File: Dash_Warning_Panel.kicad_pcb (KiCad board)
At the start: 2 copper layers, 57 x 40 mm, 30 parts, among them J1 Conn_01x06_Male, SW1 SW_DIP_x02, U1 BD2808MUV, U3 TPS22810-Q1

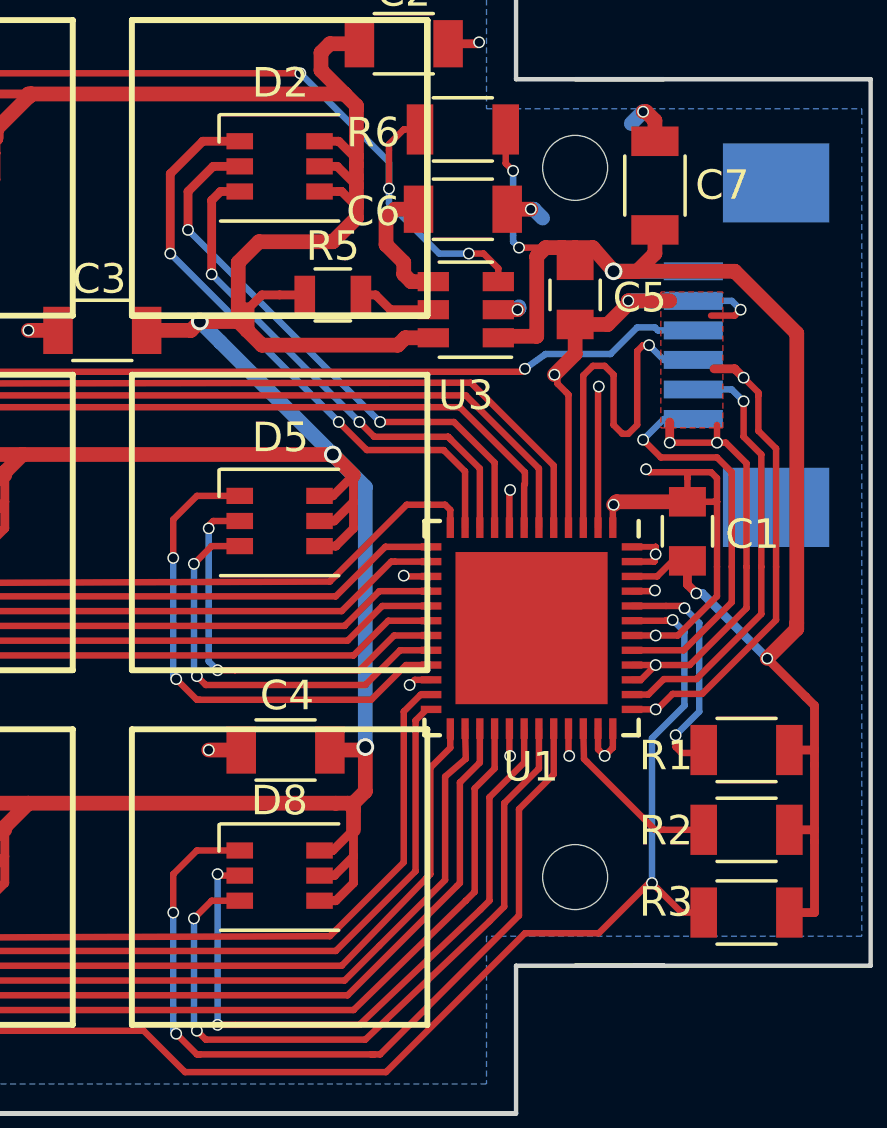
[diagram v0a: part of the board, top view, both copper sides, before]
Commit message: Fixed C6 footprint
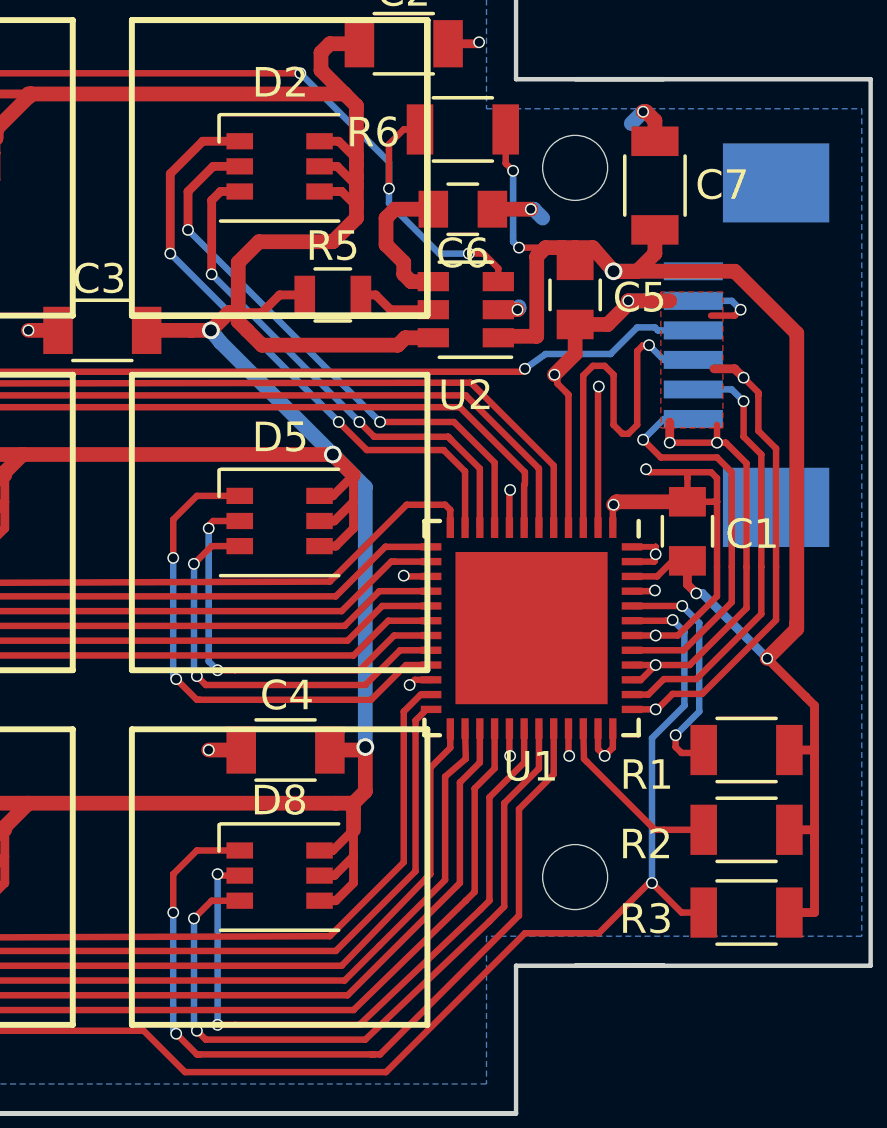
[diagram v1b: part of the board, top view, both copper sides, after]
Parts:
- C6: footprint Capacitors_SMD:C_1206 -> Capacitors_SMD:C_0805
- R2: value 10k -> 68k
- renumbered U3 to U2
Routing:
- net /LED_Power: track 174.0 -> 173.5 mm

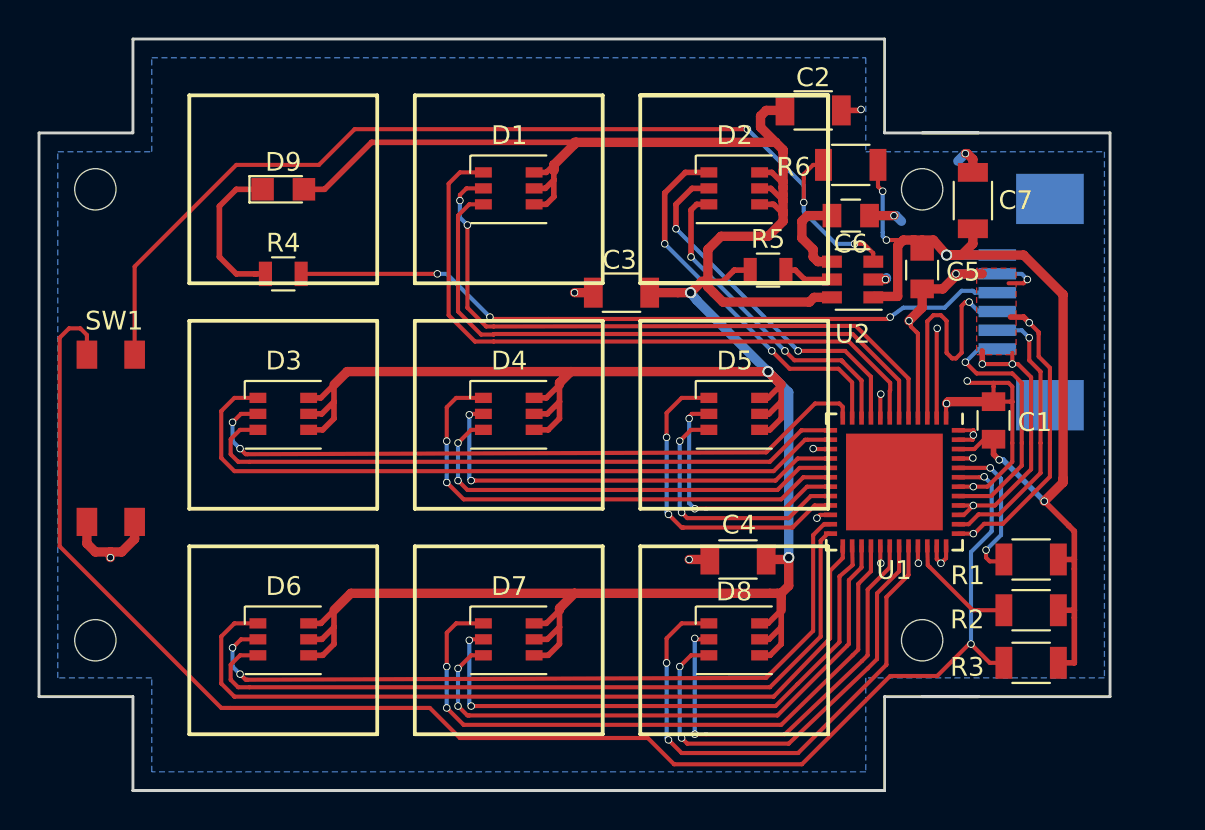
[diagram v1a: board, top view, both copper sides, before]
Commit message: Base Production
Extended Board Outline, Fixed Solder Mask overlay, added ground via's for thermal pad under U1, added flood fill capacitors for VCC and LED Power in unoccupied boardspace.
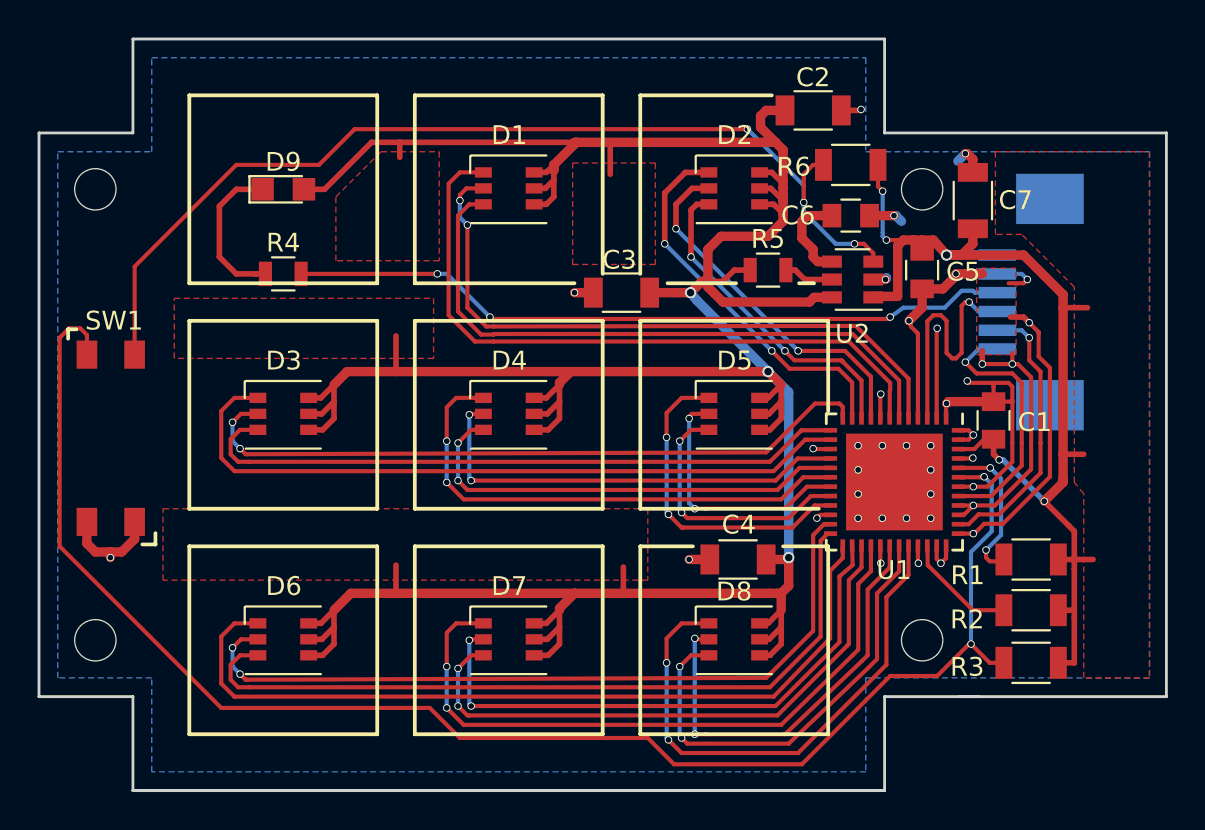
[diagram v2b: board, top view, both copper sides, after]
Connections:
- U1 pad 49: (no net) -> /GND
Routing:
- net /LED_Power: track 173.5 -> 180.8 mm
- net /VCC: track 54.7 -> 58.1 mm
- net /GND: track 89.4 -> 89.2 mm, vias 27 -> 39
- added copper zone on F.Cu, net /LED_Power
- added copper zone on F.Cu, net /VCC
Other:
- board size 57 x 40 mm -> 60 x 40 mm
- rule pad_to_mask_clearance: 0.2 -> 0.0508
- board text added: "UCONN FSAE 2019"

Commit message: Fabrication 2
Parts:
- SW1: moved to B.Cu
- moved SW1 3.50 mm to (174.5, 122.0), turned to 180 degrees
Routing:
- net /GND: track 89.2 -> 83.9 mm, vias 39 -> 38
- net /OE: track 83.0 -> 85.5 mm, vias 2 -> 3
- net /EN: track 53.8 -> 56.2 mm, vias 3 -> 4
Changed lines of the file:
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@@
-(kicad_pcb (version 4) (host pcbnew 4.0.7)
+(kicad_pcb (version 20171130) (host pcbnew "(5.0.2)-1")
   (general
-    (links 116)
-    (no_connects 0)
-    (area 152.292858 95.8 236.350001 157.7)
     (thickness 1.6)
-    (drawings 87)
-    (tracks 765)
+    (drawings 86)
+    (tracks 763)
     (zones 0)
     (modules 30)
@@
   (page A4)
   (layers
-    (0 F.Cu signal)
+    (0 F.Cu signal hide)
     (31 B.Cu signal)
     (32 B.Adhes user hide)
@@
     (39 F.Mask user hide)
     (40 Dwgs.User user hide)
-    (41 Cmts.User user hide)
+    (41 Cmts.User user)
     (42 Eco1.User user hide)
     (43 Eco2.User user hide)
     (44 Edge.Cuts user)
     (45 Margin user hide)
-    (46 B.CrtYd user hide)
-    (47 F.CrtYd user hide)
+    (46 B.CrtYd user)
+    (47 F.CrtYd user)
     (48 B.Fab user hide)
     (49 F.Fab user hide)
   )
   (setup
-    (last_trace_width 0.3)
+    (last_trace_width 0.22)
     (user_trace_width 0.3)
     (user_trace_width 0.5)
@@
     (pad_drill 0)
     (pad_to_mask_clearance 0.0508)
+    (solder_mask_min_width 0.25)
     (aux_axis_origin 0 0)
-    (visible_elements 7FFEF719)
+    (visible_elements 7FFFF719)
     (pcbplotparams
       (layerselection 0x012f0_80000001)
       (usegerberextensions true)
+      (usegerberattributes false)
+      (usegerberadvancedattributes false)
+      (creategerberjobfile false)
       (excludeedgelayer true)
       (linewidth 0.100000)
@@
       (hpglpennumber 1)
       (hpglpenspeed 20)
-      (hpglpendiameter 15)
-      (hpglpenoverlay 2)
+      (hpglpendiameter 15.000000)
       (psnegative false)
       (psa4output false)
@@
       (drillshape 0)
       (scaleselection 1)
-      (outputdirectory CAM/))
+      (outputdirectory "CAM/"))
   )
   (net 0 "")
@@
     (tags "QFN 0.5")
     (attr smd)
-    (fp_text reference U1 (at 4.696 0.022 360) (layer F.SilkS)
+    (fp_text reference U1 (at 4.696 0.022) (layer F.SilkS)
       (effects (font (size 1 1) (thickness 0.15)))
     )
@@
     )
   )
-  (module Apem:2.54mm_DIP_Switch_2_Position (layer F.Cu)
-    (at 171 122)
-    (fp_text reference SW1 (at 2 1) (layer F.SilkS)
-      (effects (font (size 1 1) (thickness 0.15)))
-    )
-    (fp_text value SW_DIP_x02 (at 2 -1) (layer F.Fab)
-      (effects (font (size 1 1) (thickness 0.15)))
-    )
-    (pad 1 smd rect (at 0.55 2.8) (size 1.1 1.5) (layers F.Cu F.Paste F.Mask)
+  (module Apem:2.54mm_DIP_Switch_2_Position (layer B.Cu)
+    (at 174.5 122 180)
+    (fp_text reference SW1 (at 2 -1 180) (layer B.SilkS)
+      (effects (font (size 1 1) (thickness 0.15)) (justify mirror))
+    )
+    (fp_text value SW_DIP_x02 (at 2 1 180) (layer B.Fab)
+      (effects (font (size 1 1) (thickness 0.15)) (justify mirror))
+    )
+    (pad 1 smd rect (at 0.55 -2.8 180) (size 1.1 1.5) (layers B.Cu B.Paste B.Mask)
       (net 33 /OE))
-    (pad 2 smd rect (at 3.09 2.8) (size 1.1 1.5) (layers F.Cu F.Paste F.Mask)
+    (pad 2 smd rect (at 3.09 -2.8 180) (size 1.1 1.5) (layers B.Cu B.Paste B.Mask)
       (net 34 /EN))
-    (pad 3 smd rect (at 0.55 11.7) (size 1.1 1.5) (layers F.Cu F.Paste F.Mask)
-      (net 37 /GND))
-    (pad 4 smd rect (at 3.09 11.7) (size 1.1 1.5) (layers F.Cu F.Paste F.Mask)
+    (pad 3 smd rect (at 0.55 -11.7 180) (size 1.1 1.5) (layers B.Cu B.Paste B.Mask)
+      (net 37 /GND))
+    (pad 4 smd rect (at 3.09 -11.7 180) (size 1.1 1.5) (layers B.Cu B.Paste B.Mask)
       (net 37 /GND))
   )
@@
   (gr_line (start 209.45 121) (end 210.25 121) (angle 90) (layer F.SilkS) (width 0.2))
   (gr_line (start 202.45 121) (end 206.1 121) (angle 90) (layer F.SilkS) (width 0.2))
-  (gr_line (start 175.2 134.9) (end 174.5 134.9) (angle 90) (layer F.SilkS) (width 0.2))
   (gr_line (start 175.2 134.3) (end 175.2 134.9) (angle 90) (layer F.SilkS) (width 0.2))
   (gr_line (start 170.55 123.45) (end 170.55 123.95) (angle 90) (layer F.SilkS) (width 0.2))
@@
   (segment (start 193.1 122.9) (end 193 122.8) (width 0.22) (layer F.Cu) (net 32))
   (segment (start 218.6 140.2) (end 218.5 140.2) (width 0.22) (layer F.Cu) (net 33))
-  (segment (start 171.55 123.75) (end 171.55 124.8) (width 0.22) (layer F.Cu) (net 33))
-  (segment (start 171.2 123.4) (end 171.55 123.75) (width 0.22) (layer F.Cu) (net 33))
   (segment (start 170.6 123.4) (end 171.2 123.4) (width 0.22) (layer F.Cu) (net 33))
   (segment (start 170.1 123.9) (end 170.6 123.4) (width 0.22) (layer F.Cu) (net 33))
@@
   (segment (start 219.7 131.7) (end 219.7 134.2) (width 0.22) (layer B.Cu) (net 33))
   (segment (start 217.925 131.325) (end 219.075 131.325) (width 0.22) (layer F.Cu) (net 33))
+  (via (at 173.9 123.5) (size 0.4) (drill 0.3) (layers F.Cu B.Cu) (net 33))
+  (segment (start 171.2 123.4) (end 173.8 123.4) (width 0.22) (layer F.Cu) (net 33))
+  (segment (start 173.8 123.4) (end 173.9 123.5) (width 0.22) (layer F.Cu) (net 33))
+  (segment (start 173.95 123.55) (end 173.95 124.8) (width 0.22) (layer B.Cu) (net 33))
+  (segment (start 173.9 123.5) (end 173.95 123.55) (width 0.22) (layer B.Cu) (net 33))
   (segment (start 209.7 116.7) (end 209.7 115.8) (width 0.22) (layer B.Cu) (net 34))
-  (segment (start 174.09 120.11) (end 174.09 124.8) (width 0.22) (layer F.Cu) (net 34))
-  (segment (start 179.5 114.7) (end 174.09 120.11) (width 0.22) (layer F.Cu) (net 34))
-  (segment (start 183.9 114.7) (end 179.5 114.7) (width 0.22) (layer F.Cu) (net 34))
-  (segment (start 185.8 112.8) (end 183.9 114.7) (width 0.22) (layer F.Cu) (net 34))
-  (segment (start 206.7 112.8) (end 185.8 112.8) (width 0.22) (layer F.Cu) (net 34))
   (via (at 206.7 112.8) (size 0.4) (drill 0.3) (layers F.Cu B.Cu) (net 34))
   (segment (start 209.7 115.8) (end 206.7 112.8) (width 0.22) (layer B.Cu) (net 34))
@@
   (segment (start 210.75 114.7) (end 210.2 114.7) (width 0.22) (layer F.Cu) (net 34))
   (segment (start 213.4 119.4) (end 213.4 119.85) (width 0.22) (layer F.Cu) (net 34))
+  (segment (start 171.4 120.6) (end 171.4 122.8) (width 0.22) (layer F.Cu) (net 34))
+  (segment (start 177.3 114.7) (end 171.4 120.6) (width 0.22) (layer F.Cu) (net 34))
+  (segment (start 183.9 114.7) (end 177.3 114.7) (width 0.22) (layer F.Cu) (net 34))
+  (segment (start 206.7 112.8) (end 185.8 112.8) (width 0.22) (layer F.Cu) (net 34))
+  (segment (start 185.8 112.8) (end 183.9 114.7) (width 0.22) (layer F.Cu) (net 34))
+  (via (at 171.4 122.8) (size 0.4) (drill 0.3) (layers F.Cu B.Cu) (net 34))
+  (segment (start 171.4 124.79) (end 171.41 124.8) (width 0.22) (layer B.Cu) (net 34))
+  (segment (start 171.4 122.8) (end 171.4 124.79) (width 0.22) (layer B.Cu) (net 34))
   (segment (start 216.298889 136.001136) (end 216.400084 136.100084) (width 0.22) (layer F.Cu) (net 35))
   (segment (start 219 138.4) (end 220.35 138.4) (width 0.22) (layer F.Cu) (net 35))
@@
   (via (at 218.7 130.3) (size 0.4) (drill 0.3) (layers F.Cu B.Cu) (net 37))
   (segment (start 218.675 130.325) (end 218.7 130.3) (width 0.22) (layer F.Cu) (net 37))
-  (segment (start 172.8 135.3) (end 172.8 135.6) (width 0.5) (layer F.Cu) (net 37))
-  (via (at 172.8 135.6) (size 0.4) (drill 0.3) (layers F.Cu B.Cu) (net 37))
-  (segment (start 171.55 133.7) (end 171.55 134.85) (width 0.5) (layer F.Cu) (net 37))
-  (segment (start 174.09 134.61) (end 174.09 133.7) (width 0.5) (layer F.Cu) (net 37))
-  (segment (start 173.4 135.3) (end 174.09 134.61) (width 0.5) (layer F.Cu) (net 37))
-  (segment (start 172 135.3) (end 172.8 135.3) (width 0.5) (layer F.Cu) (net 37))
-  (segment (start 172.8 135.3) (end 173.4 135.3) (width 0.5) (layer F.Cu) (net 37))
-  (segment (start 171.55 134.85) (end 172 135.3) (width 0.5) (layer F.Cu) (net 37))
   (segment (start 213.775 134.975) (end 213.775 135.875) (width 0.22) (layer F.Cu) (net 37))
   (via (at 213.8 135.9) (size 0.4) (drill 0.3) (layers F.Cu B.Cu) (net 37))
